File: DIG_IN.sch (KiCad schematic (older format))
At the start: 5 parts, among them U8 PC817

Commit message: Comments and Notation for clarity
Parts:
- renumbered 4.7k to 4.7k1
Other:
- note added: "Pull Up Resistor"
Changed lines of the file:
@@
 encoding utf-8
 Sheet 6 6
-Title ""
-Date ""
-Rev ""
-Comp ""
-Comment1 ""
+Title "Digital Input"
+Date "2021-05-25"
+Rev "1"
+Comp "Harsch Systems"
+Comment1 "Tyler Stowell"
 Comment2 ""
 Comment3 ""
@@
 $EndComp
 $Comp
-L Device:R_US 4.7k
+L Device:R_US 4.7k1
 U 1 1 60B2A02B
 P 5050 4400
-F 0 "4.7k" H 4982 4354 50  0000 R CNN
+F 0 "4.7k1" H 4982 4354 50  0000 R CNN
 F 1 "R_US" H 4982 4445 50  0000 R CNN
 F 2 "" V 5090 4390 50  0001 C CNN
@@
 Wire Wire Line
 	6650 4100 6850 4100
-Text Notes 4550 4050 0    50   ~ 0
+Text Notes 4500 4250 0    50   ~ 0
 Status LED
+Wire Notes Line
+	4950 3850 5350 3850
+Wire Notes Line
+	5350 3850 5350 4550
+Wire Notes Line
+	5350 4550 4950 4550
+Wire Notes Line
+	4950 4550 4950 3850
+Wire Notes Line
+	6800 3700 7500 3700
+Wire Notes Line
+	7500 3700 7500 4200
+Wire Notes Line
+	7500 4200 6800 4200
+Wire Notes Line
+	6800 4200 6800 3700
+Text Notes 6850 3650 0    50   ~ 0
+Pull Up Resistor
 $EndSCHEMATC

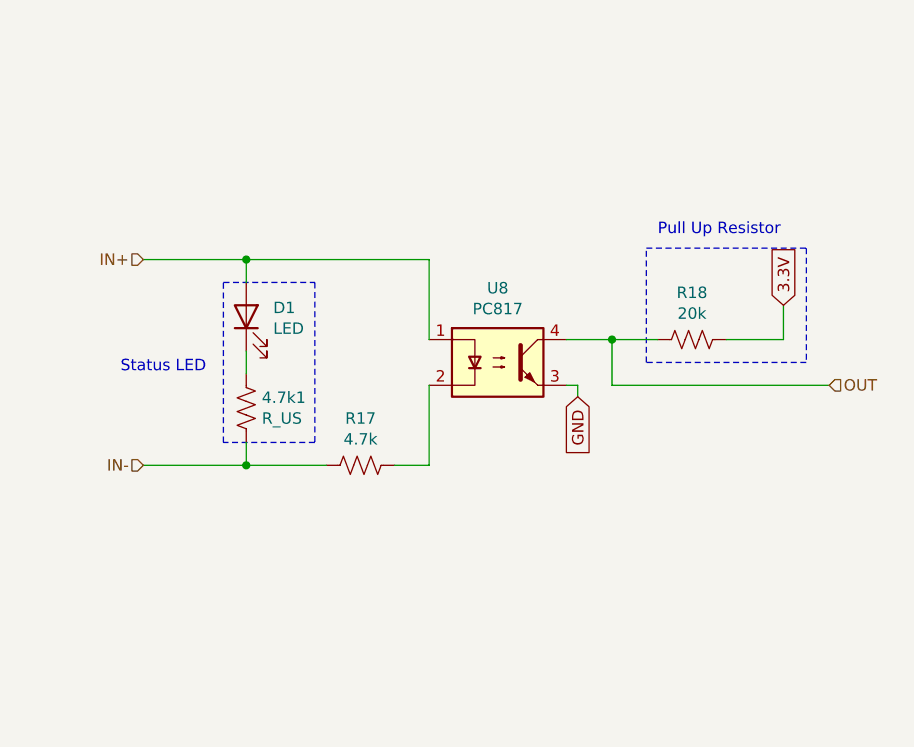
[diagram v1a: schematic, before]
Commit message: Cleanup, added second digital input, and created sheet for digital output (currently empty)
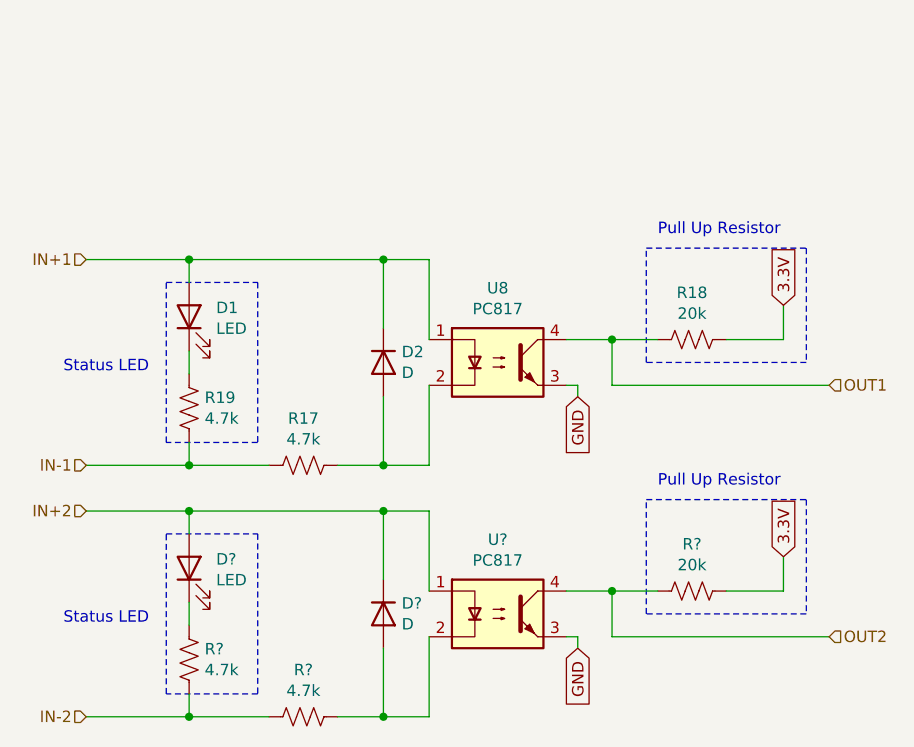
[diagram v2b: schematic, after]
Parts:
- added D2, D?: D, symbol Device:D
- added D?: LED, symbol Device:LED
- added R? (x2): 4.7k, symbol Device:R_US
- added R?: 20k, symbol Device:R_US
- added U?: PC817, Package_DIP:DIP-4_W7.62mm, symbol Isolator:PC817
- R19: renamed from 4.7k1; value R_US -> 4.7k
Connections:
- net 3.3V: now also R?.1
- net GND: now also U?.3
- net at R17.1, U8.2: now also D2.2 (A)
- net IN+ renamed IN+1
- net IN+1: now also D2.1 (K)
- net IN- renamed IN-1
- net OUT renamed OUT1
- new net: D?.1 (K), R?.2
- new net: D?.2 (A), R?.1, U?.2
- new net IN+2: D?.1 (K), D?.2 (A), U?.1
- new net IN-2: R?.1, R?.2
- new net OUT2: R?.2, U?.4
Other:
- moved on the sheet: D1, R17, R19

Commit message: Testing and adjustments
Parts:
- removed D?: LED, symbol Device:LED
- removed R19, R? (x2): 4.7k, symbol Device:R_US
- added D?: LED, symbol Device:LED
- added R?: 4.7k, symbol Device:R_US
- gave numbers to parts that had none: 3
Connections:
- net IN+1: no longer D2.1 (K), U8.1
- net IN+2: now also D?.2 (A); no longer D4.1 (K), U9.1
- net IN-2: now also R?.2
- net at D1.1 (K): now also D2.1 (K), U8.1
- net at D4.2 (A), U9.2: now also R?.1
- new net: D4.1 (K), D?.1 (K), U9.1
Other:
- moved on the sheet: D1, D2, D4, R17, R18, R22, U8, U9

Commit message: Footprint Association
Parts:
- D1: footprint (none) -> LED_THT:LED_D5.0mm
- D2: renamed from D?; footprint (none) -> LED_THT:LED_D5.0mm
- D3: renamed from D2; footprint (none) -> Diode_THT:D_A-405_P10.16mm_Horizontal
- D4: footprint (none) -> Diode_THT:D_A-405_P10.16mm_Horizontal
- R17: footprint (none) -> Resistor_THT:R_Axial_DIN0207_L6.3mm_D2.5mm_P10.16mm_Horizontal
- R18: renamed from R?; footprint (none) -> Resistor_THT:R_Axial_DIN0207_L6.3mm_D2.5mm_P10.16mm_Horizontal
- R19: renamed from R18; footprint (none) -> Resistor_THT:R_Axial_DIN0207_L6.3mm_D2.5mm_P10.16mm_Horizontal
- R20: renamed from R22; footprint (none) -> Resistor_THT:R_Axial_DIN0207_L6.3mm_D2.5mm_P10.16mm_Horizontal
- renumbered U8 to U5, U9 to U6
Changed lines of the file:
@@
 F 0 "D1" H 4843 2745 50  0000 C CNN
 F 1 "LED" H 4843 2836 50  0000 C CNN
-F 2 "" H 4850 3000 50  0001 C CNN
+F 2 "LED_THT:LED_D5.0mm" H 4850 3000 50  0001 C CNN
 F 3 "~" H 4850 3000 50  0001 C CNN
 	1    4850 3000
@@
 P 5700 3450
 AR Path="/60AC3F67/60B2C751" Ref="U?"  Part="1"
-AR Path="/60B28EA9/60B2C751" Ref="U8"  Part="1"
-F 0 "U8" H 5700 3775 50  0000 C CNN
+AR Path="/60B28EA9/60B2C751" Ref="U5"  Part="1"
+F 0 "U5" H 5700 3775 50  0000 C CNN
 F 1 "PC817" H 5700 3684 50  0000 C CNN
 F 2 "Package_DIP:DIP-4_W7.62mm" H 5500 3250 50  0001 L CIN
@@
 F 0 "R17" V 4645 3900 50  0000 C CNN
 F 1 "4.7k" V 4736 3900 50  0000 C CNN
-F 2 "" V 4890 3890 50  0001 C CNN
+F 2 "Resistor_THT:R_Axial_DIN0207_L6.3mm_D2.5mm_P10.16mm_Horizontal" V 4890 3890 50  0001 C CNN
 F 3 "~" H 4850 3900 50  0001 C CNN
 	1    4850 3900
@@
 GND
 $Comp
-L Device:R_US R18
+L Device:R_US R19
 U 1 1 60B348C0
 P 6550 3350
-F 0 "R18" V 6345 3350 50  0000 C CNN
+F 0 "R19" V 6345 3350 50  0000 C CNN
 F 1 "20k" V 6436 3350 50  0000 C CNN
-F 2 "" V 6590 3340 50  0001 C CNN
+F 2 "Resistor_THT:R_Axial_DIN0207_L6.3mm_D2.5mm_P10.16mm_Horizontal" V 6590 3340 50  0001 C CNN
 F 3 "~" H 6550 3350 50  0001 C CNN
 	1    6550 3350
@@
 Pull Up Resistor
 $Comp
-L Device:D D2
+L Device:D D3
 U 1 1 60B8ECB5
 P 5200 3450
-F 0 "D2" V 5154 3530 50  0000 L CNN
+F 0 "D3" V 5154 3530 50  0000 L CNN
 F 1 "D" V 5245 3530 50  0000 L CNN
-F 2 "" H 5200 3450 50  0001 C CNN
+F 2 "Diode_THT:D_A-405_P10.16mm_Horizontal" H 5200 3450 50  0001 C CNN
 F 3 "~" H 5200 3450 50  0001 C CNN
 	1    5200 3450
@@
 P 5700 4750
 AR Path="/60AC3F67/60B9B8C2" Ref="U?"  Part="1"
-AR Path="/60B28EA9/60B9B8C2" Ref="U9"  Part="1"
-F 0 "U9" H 5700 5075 50  0000 C CNN
+AR Path="/60B28EA9/60B9B8C2" Ref="U6"  Part="1"
+F 0 "U6" H 5700 5075 50  0000 C CNN
 F 1 "PC817" H 5700 4984 50  0000 C CNN
 F 2 "Package_DIP:DIP-4_W7.62mm" H 5500 4550 50  0001 L CIN
@@
 GND
 $Comp
-L Device:R_US R22
+L Device:R_US R20
 U 1 1 60B9B8D8
 P 6550 4650
-F 0 "R22" V 6345 4650 50  0000 C CNN
+F 0 "R20" V 6345 4650 50  0000 C CNN
 F 1 "20k" V 6436 4650 50  0000 C CNN
-F 2 "" V 6590 4640 50  0001 C CNN
+F 2 "Resistor_THT:R_Axial_DIN0207_L6.3mm_D2.5mm_P10.16mm_Horizontal" V 6590 4640 50  0001 C CNN
 F 3 "~" H 6550 4650 50  0001 C CNN
 	1    6550 4650
@@
 F 0 "D4" V 5154 4830 50  0000 L CNN
 F 1 "D" V 5245 4830 50  0000 L CNN
-F 2 "" H 5200 4750 50  0001 C CNN
+F 2 "Diode_THT:D_A-405_P10.16mm_Horizontal" H 5200 4750 50  0001 C CNN
 F 3 "~" H 5200 4750 50  0001 C CNN
 	1    5200 4750
@@
 	4650 2700 4650 3100
 $Comp
-L Device:LED D?
+L Device:LED D2
 U 1 1 60C07B1F
 P 4850 4300
-F 0 "D?" H 4843 4045 50  0000 C CNN
+F 0 "D2" H 4843 4045 50  0000 C CNN
 F 1 "LED" H 4843 4136 50  0000 C CNN
-F 2 "" H 4850 4300 50  0001 C CNN
+F 2 "LED_THT:LED_D5.0mm" H 4850 4300 50  0001 C CNN
 F 3 "~" H 4850 4300 50  0001 C CNN
 	1    4850 4300
@@
 $EndComp
 $Comp
-L Device:R_US R?
+L Device:R_US R18
 U 1 1 60C07B25
 P 4850 5200
-F 0 "R?" V 4645 5200 50  0000 C CNN
+F 0 "R18" V 4645 5200 50  0000 C CNN
 F 1 "4.7k" V 4736 5200 50  0000 C CNN
-F 2 "" V 4890 5190 50  0001 C CNN
+F 2 "Resistor_THT:R_Axial_DIN0207_L6.3mm_D2.5mm_P10.16mm_Horizontal" V 4890 5190 50  0001 C CNN
 F 3 "~" H 4850 5200 50  0001 C CNN
 	1    4850 5200

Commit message: Status LED was ruining the reverse voltage protection LED's purpose
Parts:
- removed D1, D2: LED, LED_THT:LED_D5.0mm, symbol Device:LED
- removed R18: 4.7k, Resistor_THT:R_Axial_DIN0207_L6.3mm_D2.5mm_P10.16mm_Horizontal, symbol Device:R_US
- added D? (x2): LED, LED_THT:LED_D5.0mm, symbol Device:LED
- added R? (x2): 4.7k, symbol Device:R_US
- added R?: 4.7k, Resistor_THT:R_Axial_DIN0207_L6.3mm_D2.5mm_P10.16mm_Horizontal, symbol Device:R_US
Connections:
- net IN+1: now also D3.1 (K), U5.1, D?.2 (A)
- net IN+2: now also D4.1 (K), U6.1, D?.2 (A)
- net IN-1: now also R17.1, R?.2; no longer R17.2
- net IN-2: now also R?.1, R?.2
- net at D3.2 (A), U5.2: now also R17.2; no longer R17.1
- net at D4.2 (A), U6.2: now also R?.2
- new net: D?.1 (K), R?.1 (x2)
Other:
- moved on the sheet: R17
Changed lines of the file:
@@
 Comment4 ""
 $EndDescr
-Text HLabel 4500 3000 0    50   Input ~ 0
+Text HLabel 4400 3000 0    50   Input ~ 0
 IN+1
-Text HLabel 4500 3900 0    50   Input ~ 0
+Text HLabel 4400 3900 0    50   Input ~ 0
 IN-1
-$Comp
-L Device:LED D1
-U 1 1 60B29325
-P 4850 3000
-F 0 "D1" H 4843 2745 50  0000 C CNN
-F 1 "LED" H 4843 2836 50  0000 C CNN
-F 2 "LED_THT:LED_D5.0mm" H 4850 3000 50  0001 C CNN
-F 3 "~" H 4850 3000 50  0001 C CNN
-	1    4850 3000
-	-1   0    0    1
-$EndComp
 $Comp
 L Isolator:PC817 U?
@@
 L Device:R_US R17
 U 1 1 60B3319D
-P 4850 3900
-F 0 "R17" V 4645 3900 50  0000 C CNN
-F 1 "4.7k" V 4736 3900 50  0000 C CNN
-F 2 "Resistor_THT:R_Axial_DIN0207_L6.3mm_D2.5mm_P10.16mm_Horizontal" V 4890 3890 50  0001 C CNN
-F 3 "~" H 4850 3900 50  0001 C CNN
-	1    4850 3900
-	0    1    1    0
+P 4950 3900
+F 0 "R17" V 5155 3900 50  0000 C CNN
+F 1 "4.7k" V 5064 3900 50  0000 C CNN
+F 2 "Resistor_THT:R_Axial_DIN0207_L6.3mm_D2.5mm_P10.16mm_Horizontal" V 4990 3890 50  0001 C CNN
+F 3 "~" H 4950 3900 50  0001 C CNN
+	1    4950 3900
+	0    -1   -1   0
 $EndComp
 Text GLabel 6050 3600 3    50   Input ~ 0
@@
 Wire Wire Line
 	6200 3350 6400 3350
-Text Notes 4650 3200 0    50   ~ 0
-Status LED
 Wire Notes Line
 	6350 2950 7050 2950
@@
 Wire Wire Line
 	5200 3600 5200 3900
-Connection ~ 5200 3900
-Wire Wire Line
-	5200 3900 5000 3900
 Wire Wire Line
 	5200 3300 5200 3000
 Wire Wire Line
 	5200 3000 5400 3000
-Text HLabel 4500 4300 0    50   Input ~ 0
+Text HLabel 4400 4300 0    50   Input ~ 0
 IN+2
-Text HLabel 4500 5200 0    50   Input ~ 0
+Text HLabel 4400 5200 0    50   Input ~ 0
 IN-2
 $Comp
@@
 Wire Wire Line
 	5200 4300 5400 4300
-Wire Wire Line
-	5200 3000 5000 3000
+$Comp
+L Device:LED D?
+U 1 1 60C8AFD4
+P 4700 3300
+F 0 "D?" V 4750 3150 50  0000 C CNN
+F 1 "LED" V 4650 3150 50  0000 C CNN
+F 2 "LED_THT:LED_D5.0mm" H 4700 3300 50  0001 C CNN
+F 3 "~" H 4700 3300 50  0001 C CNN
+	1    4700 3300
+	0    -1   -1   0
+$EndComp
+Text Notes 4100 3350 0    50   ~ 0
+Status LED
+Wire Notes Line
+	4550 3500 4950 3500
+Wire Notes Line
+	4950 3100 4550 3100
+Wire Notes Line
+	4550 3100 4550 3500
+Wire Notes Line
+	4950 3500 4950 3100
 Connection ~ 5200 3000
 Wire Wire Line
-	4500 3000 4700 3000
-Wire Wire Line
-	4500 3900 4700 3900
-Wire Notes Line
-	4650 3100 5050 3100
-Wire Notes Line
-	5050 3100 5050 2700
-Wire Notes Line
-	5050 2700 4650 2700
-Wire Notes Line
-	4650 2700 4650 3100
-$Comp
-L Device:LED D2
-U 1 1 60C07B1F
-P 4850 4300
-F 0 "D2" H 4843 4045 50  0000 C CNN
-F 1 "LED" H 4843 4136 50  0000 C CNN
-F 2 "LED_THT:LED_D5.0mm" H 4850 4300 50  0001 C CNN
-F 3 "~" H 4850 4300 50  0001 C CNN
-	1    4850 4300
-	-1   0    0    1
-$EndComp
-$Comp
-L Device:R_US R18
-U 1 1 60C07B25
-P 4850 5200
-F 0 "R18" V 4645 5200 50  0000 C CNN
-F 1 "4.7k" V 4736 5200 50  0000 C CNN
-F 2 "Resistor_THT:R_Axial_DIN0207_L6.3mm_D2.5mm_P10.16mm_Horizontal" V 4890 5190 50  0001 C CNN
-F 3 "~" H 4850 5200 50  0001 C CNN
-	1    4850 5200
-	0    1    1    0
-$EndComp
-Text Notes 4650 4500 0    50   ~ 0
+	4400 3000 4700 3000
+$Comp
+L Device:R_US R?
+U 1 1 60C967CD
+P 4700 3700
+F 0 "R?" H 4500 3750 50  0000 L CNN
+F 1 "4.7k" H 4450 3650 50  0000 L CNN
+F 2 "" V 4740 3690 50  0001 C CNN
+F 3 "~" H 4700 3700 50  0001 C CNN
+	1    4700 3700
+	1    0    0    -1
+$EndComp
+Wire Wire Line
+	4700 3000 4700 3150
+Connection ~ 4700 3000
+Wire Wire Line
+	4700 3000 5200 3000
+Wire Wire Line
+	4700 3450 4700 3550
+Wire Wire Line
+	4400 3900 4700 3900
+Wire Wire Line
+	4700 3850 4700 3900
+Connection ~ 4700 3900
+Wire Wire Line
+	4700 3900 4800 3900
+Wire Wire Line
+	5100 3900 5200 3900
+Connection ~ 5200 3900
+$Comp
+L Device:R_US R?
+U 1 1 60CA13C5
+P 4950 5200
+F 0 "R?" V 5155 5200 50  0000 C CNN
+F 1 "4.7k" V 5064 5200 50  0000 C CNN
+F 2 "Resistor_THT:R_Axial_DIN0207_L6.3mm_D2.5mm_P10.16mm_Horizontal" V 4990 5190 50  0001 C CNN
+F 3 "~" H 4950 5200 50  0001 C CNN
+	1    4950 5200
+	0    -1   -1   0
+$EndComp
+$Comp
+L Device:LED D?
+U 1 1 60CA13CB
+P 4700 4600
+F 0 "D?" V 4750 4450 50  0000 C CNN
+F 1 "LED" V 4650 4450 50  0000 C CNN
+F 2 "LED_THT:LED_D5.0mm" H 4700 4600 50  0001 C CNN
+F 3 "~" H 4700 4600 50  0001 C CNN
+	1    4700 4600
+	0    -1   -1   0
+$EndComp
+Wire Notes Line
+	4550 4800 4950 4800
+Wire Notes Line
+	4950 4400 4550 4400
+Wire Notes Line
+	4550 4400 4550 4800
+Wire Notes Line
+	4950 4800 4950 4400
+Wire Wire Line
+	4400 4300 4700 4300
+$Comp
+L Device:R_US R?
+U 1 1 60CA13D6
+P 4700 5000
+F 0 "R?" H 4500 5050 50  0000 L CNN
+F 1 "4.7k" H 4450 4950 50  0000 L CNN
+F 2 "" V 4740 4990 50  0001 C CNN
+F 3 "~" H 4700 5000 50  0001 C CNN
+	1    4700 5000
+	1    0    0    -1
+$EndComp
+Wire Wire Line
+	4700 4300 4700 4450
+Connection ~ 4700 4300
+Wire Wire Line
+	4700 4300 5200 4300
+Wire Wire Line
+	4700 4750 4700 4850
+Wire Wire Line
+	4400 5200 4700 5200
+Wire Wire Line
+	4700 5150 4700 5200
+Connection ~ 4700 5200
+Wire Wire Line
+	4700 5200 4800 5200
+Wire Wire Line
+	5100 5200 5200 5200
+Connection ~ 5200 5200
+Text Notes 4100 4650 0    50   ~ 0
 Status LED
-Wire Wire Line
-	5200 5200 5000 5200
-Wire Wire Line
-	5200 4300 5000 4300
-Wire Wire Line
-	4500 4300 4700 4300
-Wire Wire Line
-	4500 5200 4700 5200
-Wire Notes Line
-	4650 4400 5050 4400
-Wire Notes Line
-	5050 4400 5050 4000
-Wire Notes Line
-	5050 4000 4650 4000
-Wire Notes Line
-	4650 4000 4650 4400
-Connection ~ 5200 4300
-Connection ~ 5200 5200
 $EndSCHEMATC
